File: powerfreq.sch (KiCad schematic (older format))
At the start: 22 parts, among them P1 CONN_01X02, Q1 2N3904, Q2 2N3904

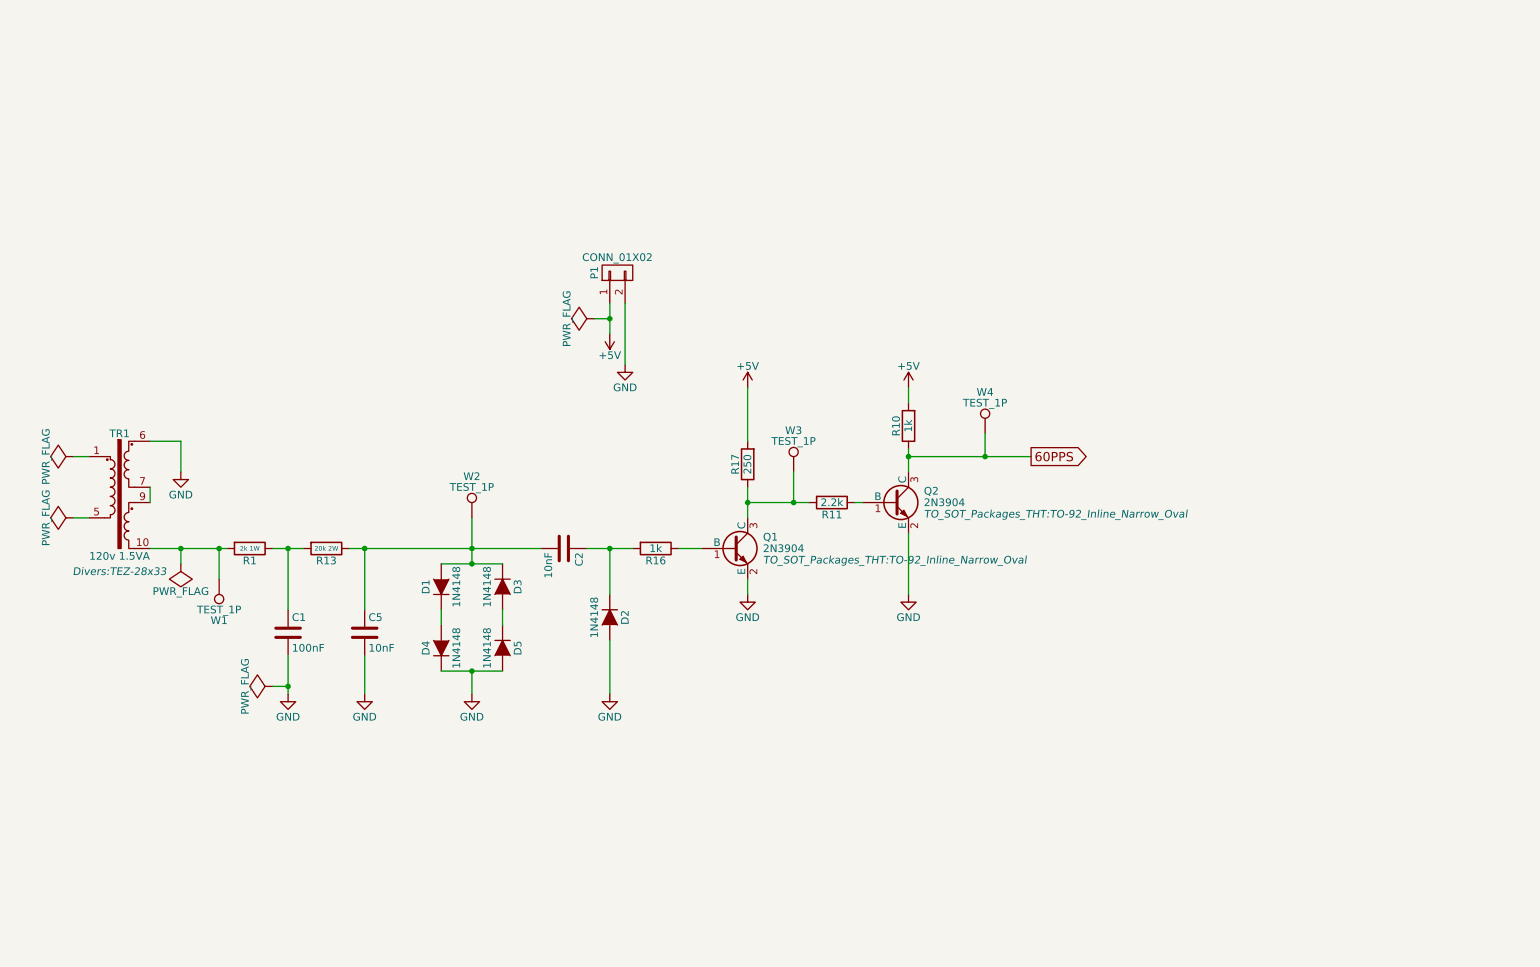
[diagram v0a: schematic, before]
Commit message: add picPET chip and SMA connector
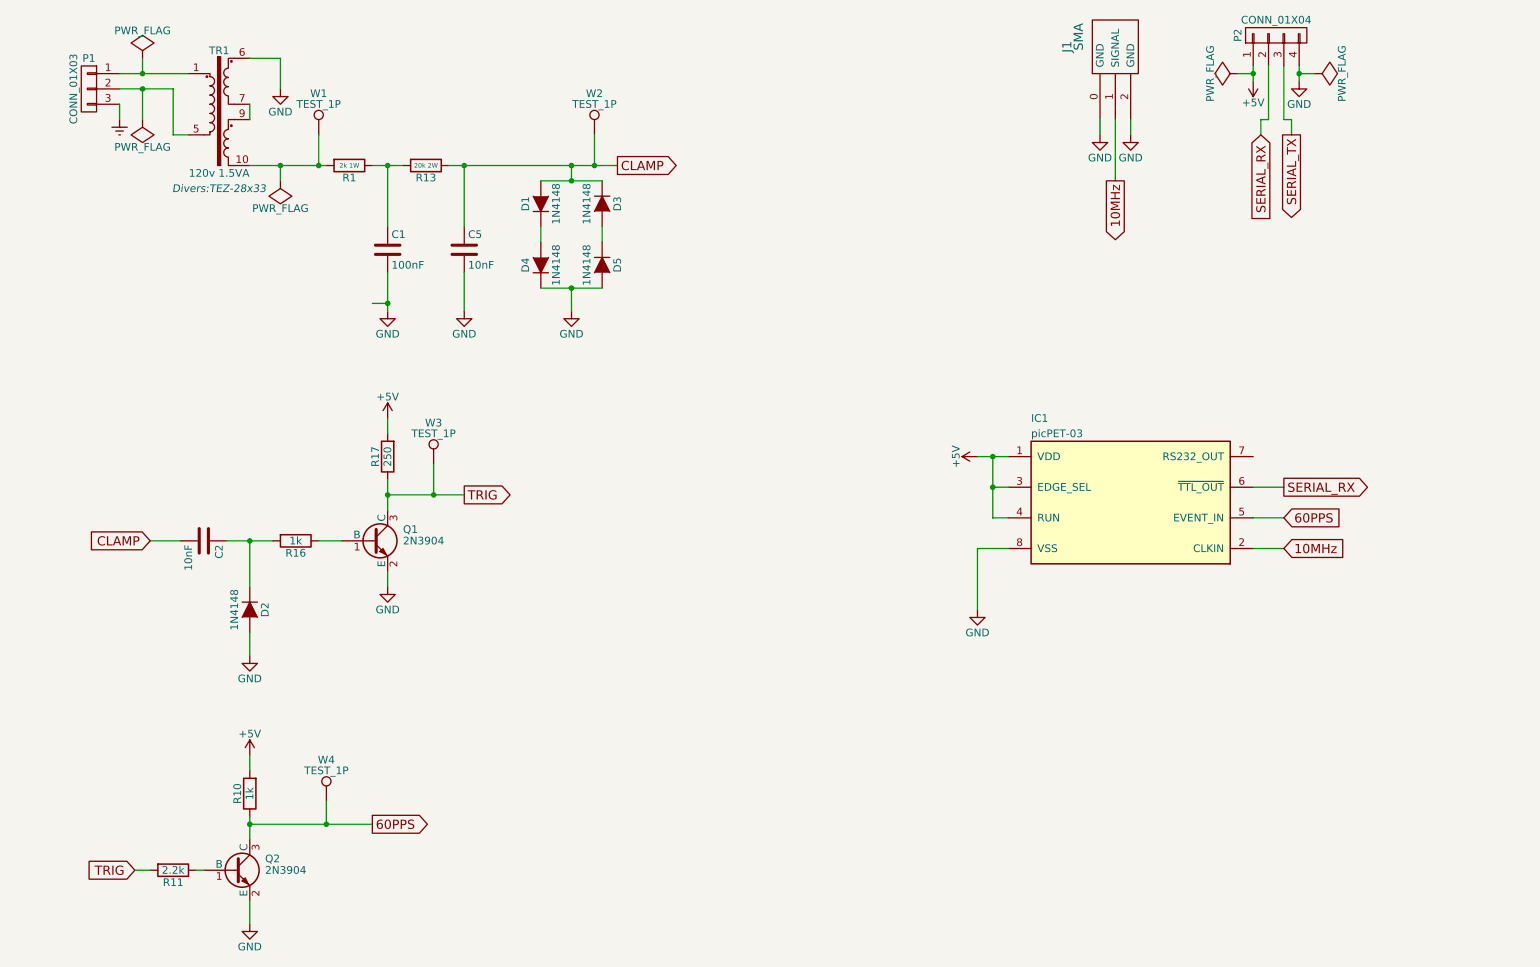
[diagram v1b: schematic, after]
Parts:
- removed P1: CONN_01X02, Pin_Headers:Pin_Header_Straight_1x02, symbol CONN_01X02
- added IC1: picPET-03, Housings_DIP:DIP-8_W7.62mm_LongPads, symbol picPET-03
- added J1: SMA, SMA_EDGE:SMA_EDGE, symbol SMA_EDGE
- added P1: CONN_01X03, Connect:Banana_Jack_3Pin, symbol CONN_01X03
- added P2: CONN_01X04, Pin_Headers:Pin_Header_Straight_1x04, symbol CONN_01X04
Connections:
- net +5V: now also IC1.1 (VDD), IC1.3 (EDGE_SEL), IC1.4 (RUN), P2.1 (P1)
- net 60PPS: now also IC1.5 (EVENT_IN)
- net GND: now also IC1.8 (VSS), J1.0 (GND), J1.2 (GND), P2.4 (P4)
- net at TR1.1: now also P1.1 (P1)
- net at TR1.5: now also P1.2 (P2)
- net CLAMP: now reaches C2.2, C5.1, D1.2 (A), D3.1 (K), R13.1, W2.1
- net TRIG: now reaches Q1.3 (C), R11.2, R17.1, W3.1
- new net 10MHz: IC1.2 (CLKIN), J1.1 (SIGNAL)
- new net Earth: P1.3 (P3)
- new net SERIAL_RX: IC1.6 (~TTL_OUT~), P2.2 (P2)
- new net SERIAL_TX: P2.3 (P3)
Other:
- moved on the sheet: C1, C2, C5, D1, D2, D3, D4, D5, Q1, Q2, R1, R10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

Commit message: Beginnings of proper layout, new footprints for transformer and picPET.
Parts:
- added C10: 100nF, Capacitors_ThroughHole:C_Rect_L7_W2.5_P5, symbol C
- added F1: 50mA, Fuse_Holders_and_Fuses:Fuseholder_Fuse_TR5_Littlefuse-No560_No460, symbol F_Small
- C1, C2, C5: footprint Capacitors_ThroughHole:C_Disc_D7.5_P5 -> Capacitors_ThroughHole:C_Rect_L7_W2.5_P5
- P1: footprint Connect:Banana_Jack_3Pin -> Wire_Connections_Bridges:WireConnection_2.00mmDrill; symbol CONN_01X03 -> CONN_01X02
- R1, R10, R11, R13, R16, R17: footprint Resistors_ThroughHole:Resistor_Horizontal_RM15mm -> Resistors_ThroughHole:Resistor_Horizontal_RM10mm
- TR1: value 120v 1.5VA -> 120v 1.2VA; footprint Divers:TEZ-28x33 -> transformers-hammond:161E120; symbol TEZ1.5-D-2 -> HAMMOND-161E120
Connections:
- net +5V: now also C10.2
- net GND: now also TR1.3, C10.1; no longer TR1.6
- net at TR1.1: now also F1.2; no longer P1.1 (P1)
- net at R1.2, W1.1: now also TR1.6; no longer TR1.10
- net at P1.2 (P2): now also TR1.2; no longer TR1.5
- removed net Earth: P1.3 (P3)
- new net: TR1.4, TR1.5
- new net: F1.1, P1.1 (P1)
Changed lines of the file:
@@
 LIBS:picpet
 LIBS:SMA_EDGE
+LIBS:transformers-hammond
 LIBS:powerfreq-cache
 EELAYER 25 0
@@
 $EndDescr
 $Comp
-L TEZ1.5-D-2 TR1
+L HAMMOND-161E120 TR1
 U 1 1 57110439
 P 2050 1400
 F 0 "TR1" H 2050 1750 50  0000 C CNN
-F 1 "120v 1.5VA" H 2050 950 50  0000 C CNN
-F 2 "Divers:TEZ-28x33" H 2050 850 50  0000 C CIN
+F 1 "120v 1.2VA" H 2050 950 50  0000 C CNN
+F 2 "transformers-hammond:161E120" H 2050 850 50  0001 C CIN
 F 3 "" H 2050 1400 50  0000 C CNN
 	1    2050 1400
@@
 F 0 "R1" V 2980 1800 50  0000 C CNN
 F 1 "2k 1W" V 2900 1800 30  0000 C CNN
-F 2 "Resistors_ThroughHole:Resistor_Horizontal_RM15mm" V 2830 1800 50  0001 C CNN
+F 2 "Resistors_ThroughHole:Resistor_Horizontal_RM10mm" V 2830 1800 50  0001 C CNN
 F 3 "" H 2900 1800 50  0000 C CNN
 	1    2900 1800
@@
 F 0 "R13" V 3480 1800 50  0000 C CNN
 F 1 "20k 2W" V 3400 1800 30  0000 C CNN
-F 2 "Resistors_ThroughHole:Resistor_Horizontal_RM15mm" V 3330 1800 50  0001 C CNN
+F 2 "Resistors_ThroughHole:Resistor_Horizontal_RM10mm" V 3330 1800 50  0001 C CNN
 F 3 "" H 3400 1800 50  0000 C CNN
 	1    3400 1800
@@
 F 0 "C1" H 3175 2450 50  0000 L CNN
 F 1 "100nF" H 3175 2250 50  0000 L CNN
-F 2 "Capacitors_ThroughHole:C_Disc_D7.5_P5" H 3188 2200 50  0001 C CNN
+F 2 "Capacitors_ThroughHole:C_Rect_L7_W2.5_P5" H 3188 2200 50  0001 C CNN
 F 3 "" H 3150 2350 50  0000 C CNN
 	1    3150 2350
@@
 F 0 "C5" H 3675 2450 50  0000 L CNN
 F 1 "10nF" H 3675 2250 50  0000 L CNN
-F 2 "Capacitors_ThroughHole:C_Disc_D7.5_P5" H 3688 2200 50  0001 C CNN
+F 2 "Capacitors_ThroughHole:C_Rect_L7_W2.5_P5" H 3688 2200 50  0001 C CNN
 F 3 "" H 3650 2350 50  0000 C CNN
 	1    3650 2350
@@
 F 0 "C2" H 1975 4350 50  0000 L CNN
 F 1 "10nF" H 1975 4150 50  0000 L CNN
-F 2 "Capacitors_ThroughHole:C_Disc_D7.5_P5" H 1988 4100 50  0001 C CNN
+F 2 "Capacitors_ThroughHole:C_Rect_L7_W2.5_P5" H 1988 4100 50  0001 C CNN
 F 3 "" H 1950 4250 50  0000 C CNN
 	1    1950 4250
@@
 F 0 "R16" V 2630 4250 50  0000 C CNN
 F 1 "1k" V 2550 4250 50  0000 C CNN
-F 2 "Resistors_ThroughHole:Resistor_Horizontal_RM15mm" V 2480 4250 50  0001 C CNN
+F 2 "Resistors_ThroughHole:Resistor_Horizontal_RM10mm" V 2480 4250 50  0001 C CNN
 F 3 "" H 2550 4250 50  0000 C CNN
 	1    2550 4250
@@
 F 0 "R17" V 3230 3700 50  0000 C CNN
 F 1 "250" V 3150 3700 50  0000 C CNN
-F 2 "Resistors_ThroughHole:Resistor_Horizontal_RM15mm" V 3080 3700 50  0001 C CNN
+F 2 "Resistors_ThroughHole:Resistor_Horizontal_RM10mm" V 3080 3700 50  0001 C CNN
 F 3 "" H 3150 3700 50  0000 C CNN
 	1    3150 3700
@@
 F 0 "R11" V 1830 6400 50  0000 C CNN
 F 1 "2.2k" V 1750 6400 50  0000 C CNN
-F 2 "Resistors_ThroughHole:Resistor_Horizontal_RM15mm" V 1680 6400 50  0001 C CNN
+F 2 "Resistors_ThroughHole:Resistor_Horizontal_RM10mm" V 1680 6400 50  0001 C CNN
 F 3 "" H 1750 6400 50  0000 C CNN
 	1    1750 6400
@@
 F 0 "R10" V 2330 5900 50  0000 C CNN
 F 1 "1k" V 2250 5900 50  0000 C CNN
-F 2 "Resistors_ThroughHole:Resistor_Horizontal_RM15mm" V 2180 5900 50  0001 C CNN
+F 2 "Resistors_ThroughHole:Resistor_Horizontal_RM10mm" V 2180 5900 50  0001 C CNN
 F 3 "" H 2250 5900 50  0000 C CNN
 	1    2250 5900
@@
 TRIG
 $Comp
-L CONN_01X03 P1
+L CONN_01X02 P1
 U 1 1 571315A0
-P 1200 1300
-F 0 "P1" H 1200 1500 50  0000 C CNN
-F 1 "CONN_01X03" V 1300 1300 50  0000 C CNN
-F 2 "Connect:Banana_Jack_3Pin" H 1200 1300 50  0001 C CNN
-F 3 "" H 1200 1300 50  0000 C CNN
-	1    1200 1300
+P 850 1250
+F 0 "P1" H 850 1450 50  0000 C CNN
+F 1 "CONN_01X03" V 950 1250 50  0000 C CNN
+F 2 "Wire_Connections_Bridges:WireConnection_2.00mmDrill" H 850 1250 50  0001 C CNN
+F 3 "" H 850 1250 50  0000 C CNN
+	1    850  1250
 	-1   0    0    -1
 $EndComp
 $Comp
-L Earth #PWR015
-U 1 1 571319E6
-P 1400 1500
-F 0 "#PWR015" H 1400 1250 50  0001 C CNN
-F 1 "Earth" H 1400 1350 50  0001 C CNN
-F 2 "" H 1400 1500 50  0000 C CNN
-F 3 "" H 1400 1500 50  0000 C CNN
-	1    1400 1500
-	1    0    0    -1
-$EndComp
-$Comp
-L PWR_FLAG #FLG016
+L PWR_FLAG #FLG015
 U 1 1 57131A7D
 P 1550 1100
-F 0 "#FLG016" H 1550 1195 50  0001 C CNN
+F 0 "#FLG015" H 1550 1195 50  0001 C CNN
 F 1 "PWR_FLAG" H 1550 1280 50  0000 C CNN
 F 2 "" H 1550 1100 50  0000 C CNN
@@
 $EndComp
 $Comp
-L PWR_FLAG #FLG017
+L PWR_FLAG #FLG016
 U 1 1 57131AD4
 P 1550 1500
-F 0 "#FLG017" H 1550 1595 50  0001 C CNN
+F 0 "#FLG016" H 1550 1595 50  0001 C CNN
 F 1 "PWR_FLAG" H 1550 1680 50  0000 C CNN
 F 2 "" H 1550 1500 50  0000 C CNN
@@
 $EndComp
 $Comp
-L +5V #PWR018
+L +5V #PWR017
 U 1 1 571324C0
 P 7000 3700
-F 0 "#PWR018" H 7000 3550 50  0001 C CNN
+F 0 "#PWR017" H 7000 3550 50  0001 C CNN
 F 1 "+5V" H 7000 3840 50  0000 C CNN
 F 2 "" H 7000 3700 50  0000 C CNN
@@
 $EndComp
 $Comp
-L GND #PWR019
+L GND #PWR018
 U 1 1 57132668
 P 7000 4700
-F 0 "#PWR019" H 7000 4450 50  0001 C CNN
+F 0 "#PWR018" H 7000 4450 50  0001 C CNN
 F 1 "GND" H 7000 4550 50  0000 C CNN
 F 2 "" H 7000 4700 50  0000 C CNN
@@
 	1400 1200 1850 1200
 Wire Wire Line
-	1400 1300 1750 1300
+	1050 1300 1750 1300
 Wire Wire Line
 	1750 1300 1750 1600
 Wire Wire Line
 	1750 1600 1850 1600
-Wire Wire Line
-	1400 1500 1400 1400
 Wire Wire Line
 	1550 1300 1550 1500
@@
 Wire Wire Line
 	7200 3900 7100 3900
-Wire Wire Line
-	7100 3700 7100 4100
 Connection ~ 7100 3700
 Wire Wire Line
@@
 $EndComp
 $Comp
-L GND #PWR020
+L GND #PWR019
 U 1 1 57134334
 P 7800 1600
-F 0 "#PWR020" H 7800 1350 50  0001 C CNN
+F 0 "#PWR019" H 7800 1350 50  0001 C CNN
 F 1 "GND" H 7800 1450 50  0000 C CNN
 F 2 "" H 7800 1600 50  0000 C CNN
@@
 $EndComp
 $Comp
-L GND #PWR021
+L GND #PWR020
 U 1 1 57134B98
 P 8000 1600
-F 0 "#PWR021" H 8000 1350 50  0001 C CNN
+F 0 "#PWR020" H 8000 1350 50  0001 C CNN
 F 1 "GND" H 8000 1450 50  0000 C CNN
 F 2 "" H 8000 1600 50  0000 C CNN
@@
 Wire Wire Line
 	8000 1600 8000 1500
+$Comp
+L F_Small F1
+U 1 1 5714335E
+P 1300 1200
+F 0 "F1" H 1260 1260 50  0000 L CNN
+F 1 "50mA" H 1180 1140 50  0000 L CNN
+F 2 "Fuse_Holders_and_Fuses:Fuseholder_Fuse_TR5_Littlefuse-No560_No460" H 1300 1200 50  0001 C CNN
+F 3 "" H 1300 1200 50  0000 C CNN
+	1    1300 1200
+	1    0    0    -1
+$EndComp
+Wire Wire Line
+	1050 1200 1200 1200
+$Comp
+L C C10
+U 1 1 571497CC
+P 7100 3200
+F 0 "C10" H 7125 3300 50  0000 L CNN
+F 1 "100nF" H 7125 3100 50  0000 L CNN
+F 2 "Capacitors_ThroughHole:C_Rect_L7_W2.5_P5" H 7138 3050 50  0001 C CNN
+F 3 "" H 7100 3200 50  0000 C CNN
+	1    7100 3200
+	1    0    0    -1
+$EndComp
+$Comp
+L GND #PWR?
+U 1 1 57149A8C
+P 7100 2950
+F 0 "#PWR?" H 7100 2700 50  0001 C CNN
+F 1 "GND" H 7100 2800 50  0000 C CNN
+F 2 "" H 7100 2950 50  0000 C CNN
+F 3 "" H 7100 2950 50  0000 C CNN
+	1    7100 2950
+	-1   0    0    1
+$EndComp
+Wire Wire Line
+	7100 3350 7100 4100
+Wire Wire Line
+	7100 3050 7100 2950
 $EndSCHEMATC

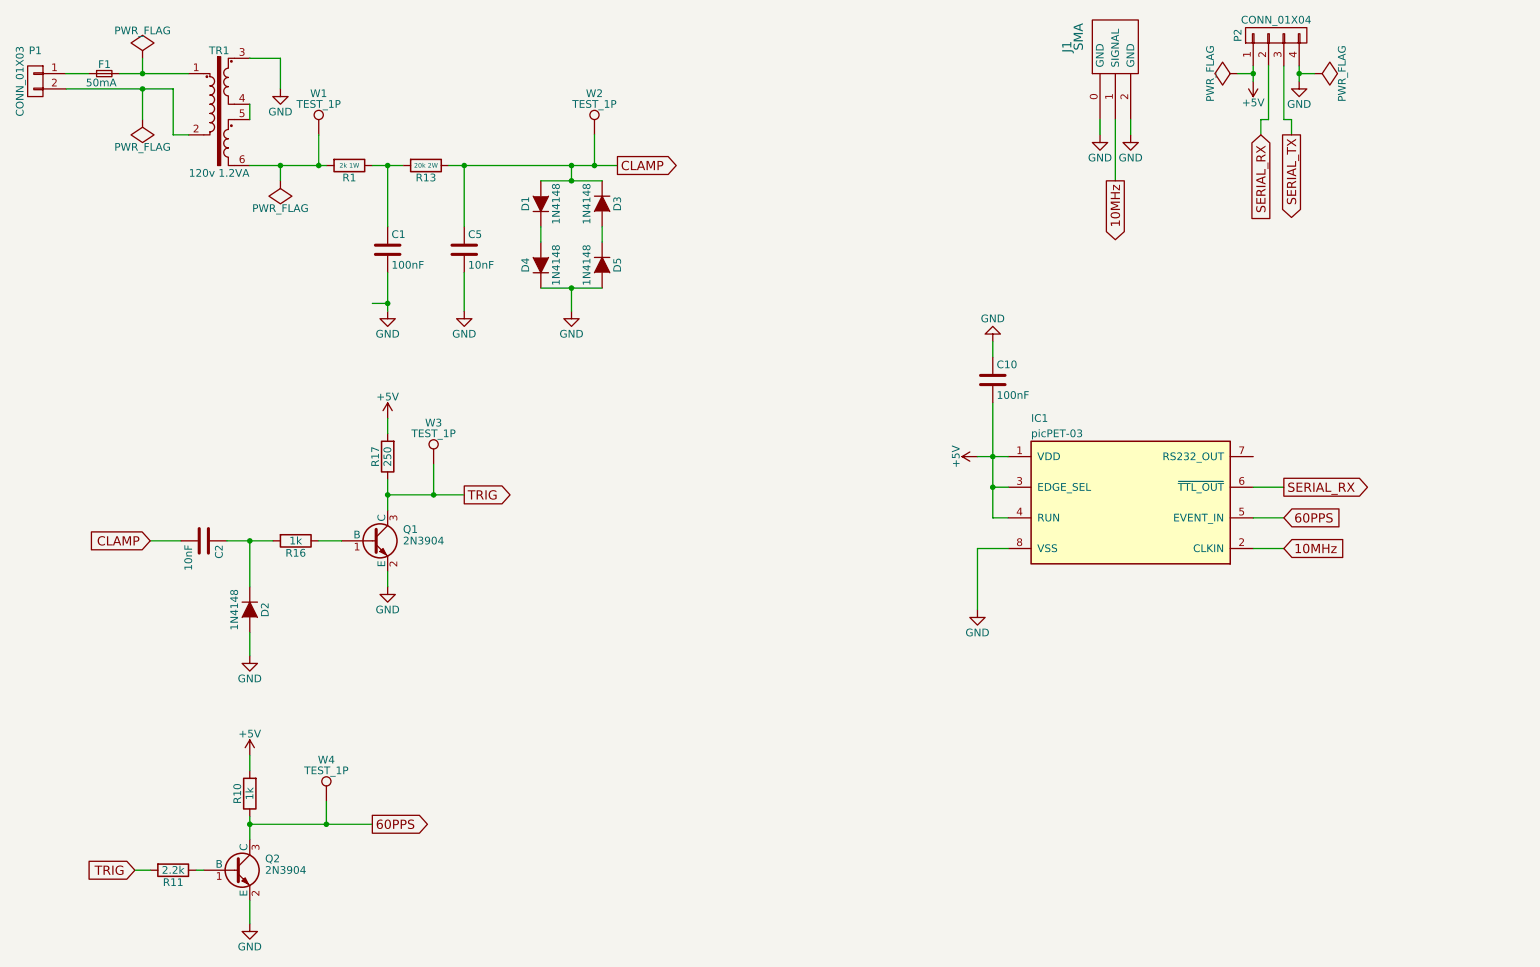
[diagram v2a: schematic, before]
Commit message: Set up layout for Hammond RL6335 box, add FTDI daughter board, and footprint fixups.
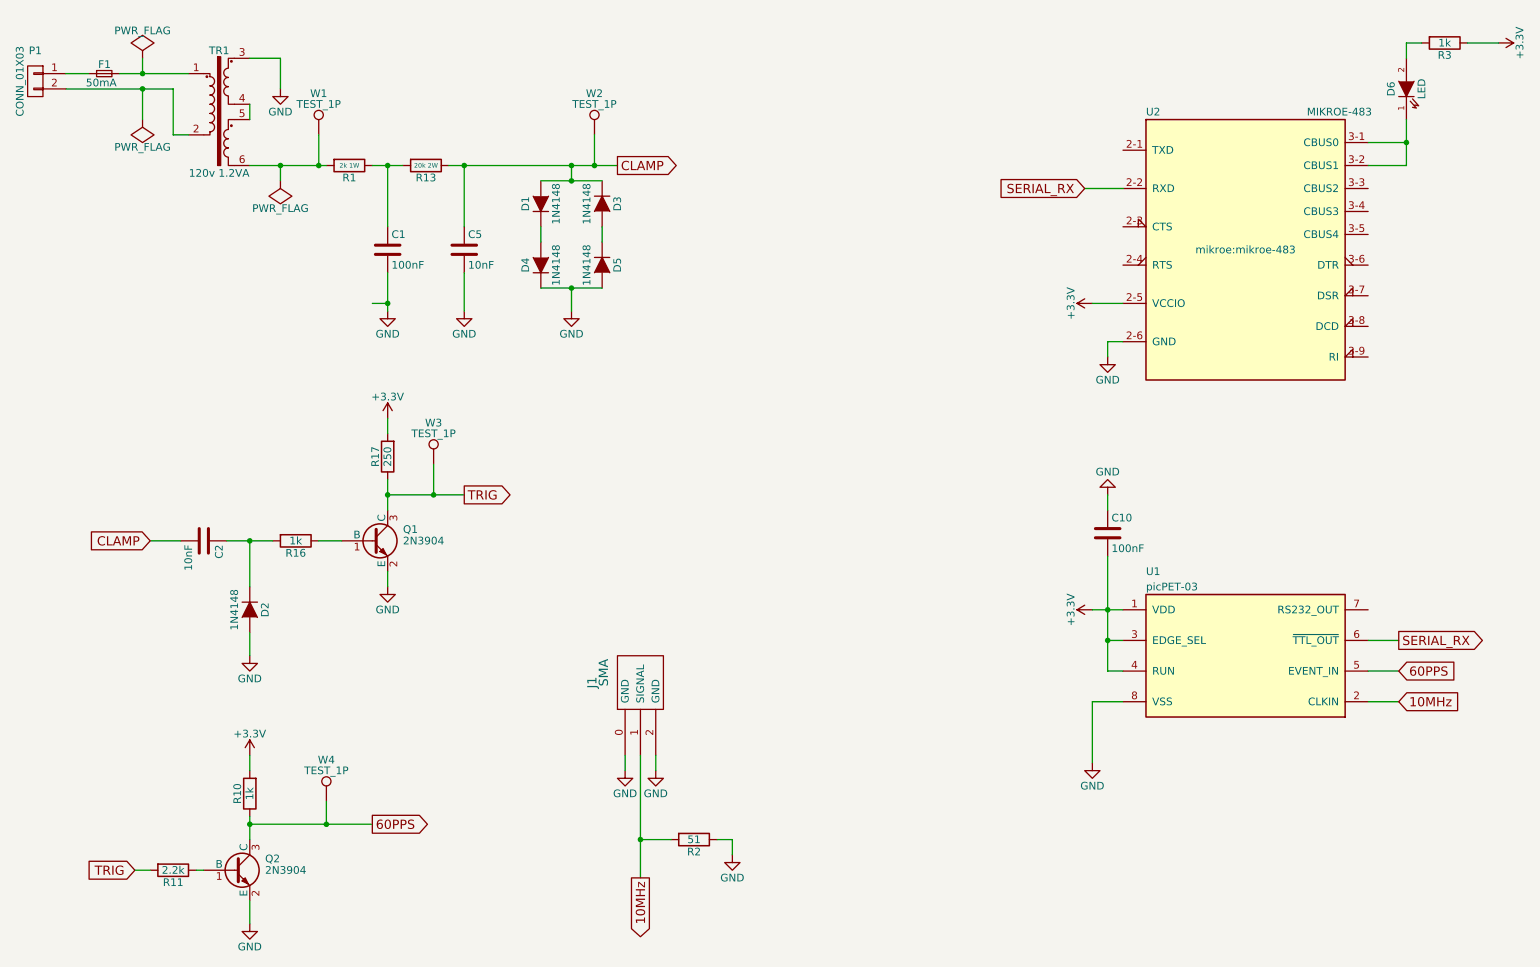
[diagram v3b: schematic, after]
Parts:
- removed P2: CONN_01X04, Pin_Headers:Pin_Header_Straight_1x04, symbol CONN_01X04
- added D6: LED, LEDs:LED-3MM, symbol LED
- added R2: 51, Resistors_ThroughHole:Resistor_Horizontal_RM10mm, symbol R
- added R3: 1k, Resistors_ThroughHole:Resistor_Horizontal_RM10mm, symbol R
- added U2: MIKROE-483, mikroe:mikroe-483, symbol MIKROE-483
- renumbered IC1 to U1
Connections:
- net 10MHz: now also R2.2
- net GND: now also R2.1, U2.2-6 (GND)
- net SERIAL_RX: now also U2.2-2 (RXD)
- net +5V renamed +3V3
- net +3V3: now also R3.1, U2.2-5 (VCCIO)
- new net: D6.1 (K), U2.3-1 (CBUS0), U2.3-2 (CBUS1)
- new net: D6.2 (A), R3.2
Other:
- moved on the sheet: C10, J1, U1

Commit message: Add track routing, and a few other fixups.
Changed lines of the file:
@@
 Connection ~ 2700 1800
-Wire Wire Line
-	3050 2700 3150 2700
-Connection ~ 3150 2700
 Wire Wire Line
 	2450 1900 2450 1800
